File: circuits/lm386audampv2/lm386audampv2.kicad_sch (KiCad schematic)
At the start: 14 parts, among them J1 Power 6 - 12 V, J2 Input, J3 Output, U1 LM386

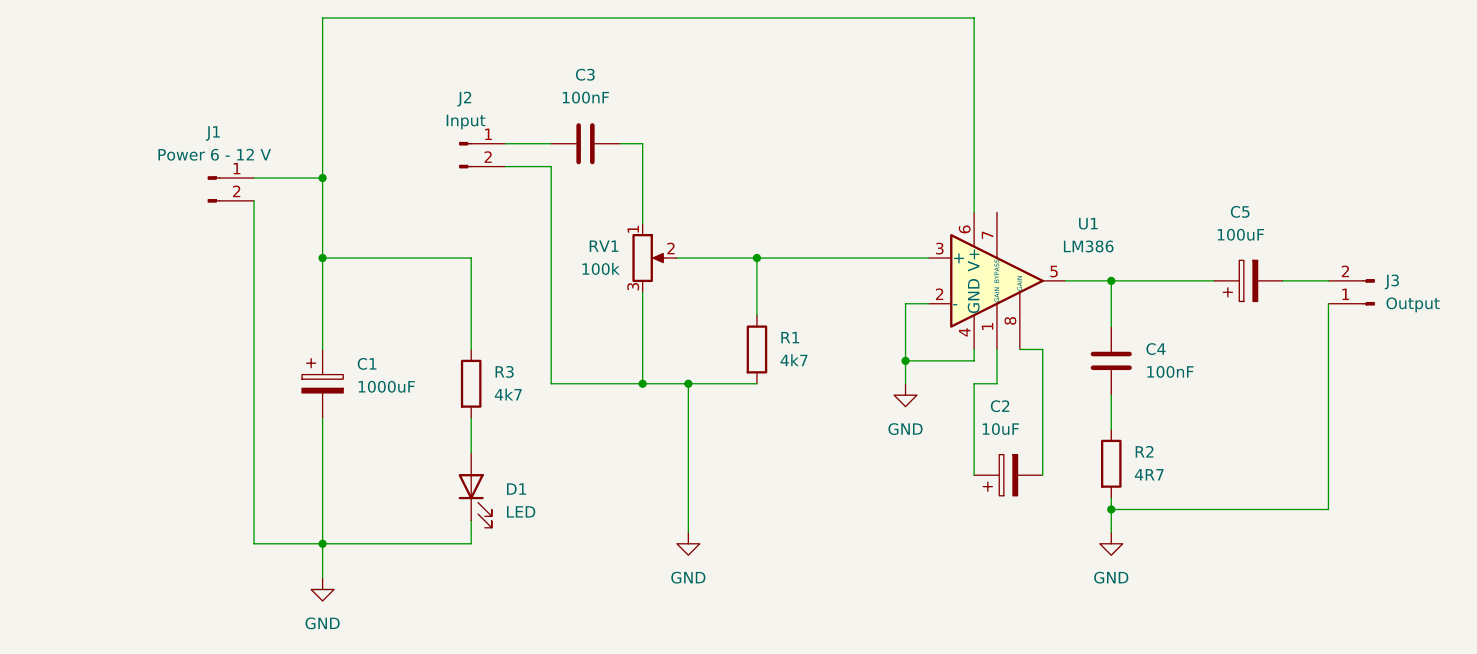
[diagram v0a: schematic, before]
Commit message: Updating the LM386 audio amplifier and adding some info images for SMD kits
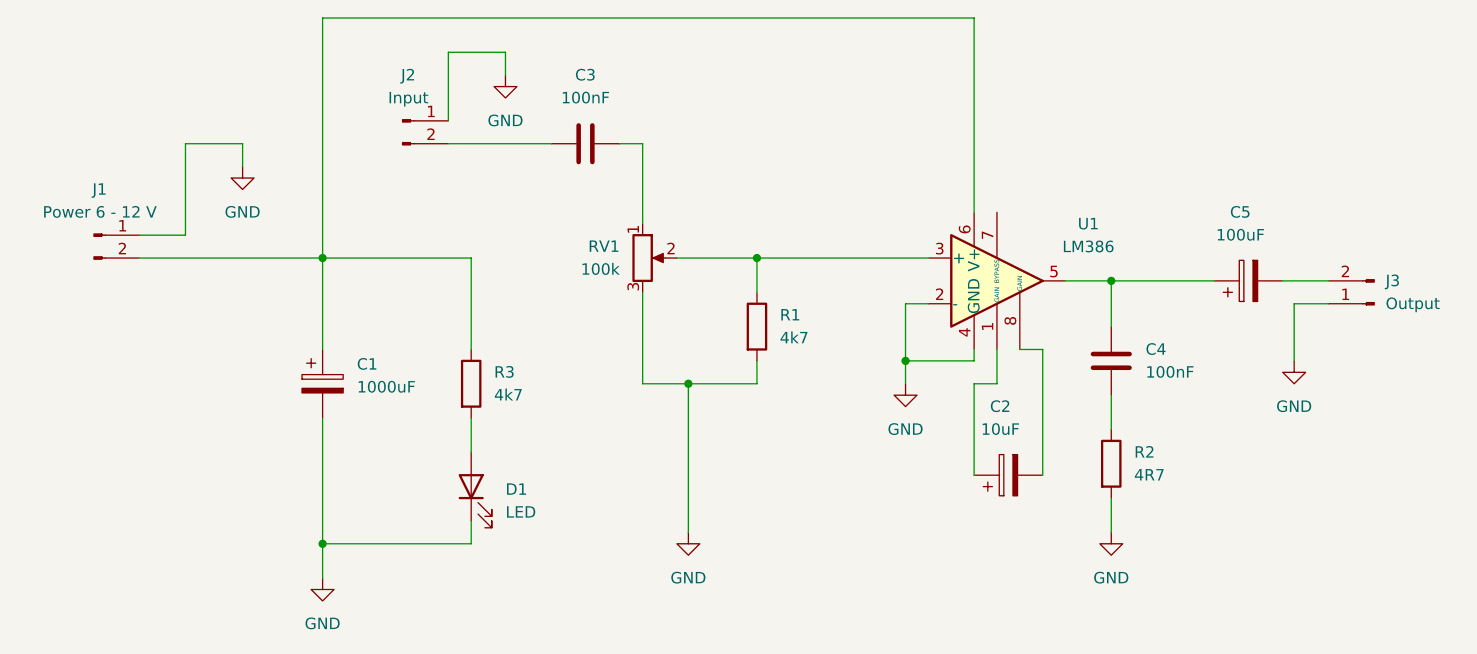
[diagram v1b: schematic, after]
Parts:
- C1: footprint (none) -> Capacitor_SMD:CP_Elec_10x10.5
- C2: footprint (none) -> Capacitor_SMD:C_1206_3216Metric_Pad1.33x1.80mm_HandSolder
- C3, C4: footprint (none) -> Capacitor_SMD:C_0805_2012Metric_Pad1.18x1.45mm_HandSolder
- C5: footprint (none) -> Capacitor_SMD:CP_Elec_5x5.4
- D1: footprint (none) -> LED_SMD:LED_1206_3216Metric_Pad1.42x1.75mm_HandSolder
- J1, J2, J3: footprint (none) -> Connector_PinHeader_2.54mm:PinHeader_1x02_P2.54mm_Vertical
- R1, R2, R3: footprint (none) -> Resistor_SMD:R_1206_3216Metric_Pad1.30x1.75mm_HandSolder
- RV1: footprint (none) -> Potentiometer_THT:Potentiometer_Alps_RK163_Single_Horizontal
- U1: footprint (none) -> Package_SO:SOIC-8_3.9x4.9mm_P1.27mm
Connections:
- net GND: now also J1.1 (Pin_1), J2.1 (Pin_1); no longer J1.2 (Pin_2), J2.2 (Pin_2)
- net at C3.1: now also J2.2 (Pin_2); no longer J2.1 (Pin_1)
- net at C1.1, R3.1, U1.6 (V+): now also J1.2 (Pin_2); no longer J1.1 (Pin_1)
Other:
- moved on the sheet: J1, J2, R1
